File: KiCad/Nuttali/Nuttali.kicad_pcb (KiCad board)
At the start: 2 copper layers, 52.7 x 101.7 mm, 85 parts, among them J1 SWD, J2 B4B-XH-A, SW1 SW_DPST_x2, SW10 SW_Push, SW2 RND 210-00662, SW3 SW_Push, SW4 SW_Push, SW5 SW_Push, SW6 SW_Push, SW7 SW_Push, SW8 Rotary_Encoder, U1 STM32F411RETx, U2 PMW3389, U3 USBLC6-2P6, U4 AP131-15, U5 AP1117-15, Y1 16Mhz

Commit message: Working on the new pcb
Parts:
- removed D1, D4: LED, LED_SMD:LED_0201_0603Metric_Pad0.64x0.40mm_HandSolder
- added J3: Conn_01x03_Male, Connector_PinSocket_2.54mm:PinSocket_1x03_P2.54mm_Vertical, F.Cu at (192.0, 117.3)
- added J4: Conn_01x03_Male, Connector_PinSocket_2.54mm:PinSocket_1x03_P2.54mm_Vertical, F.Cu at (192.0, 99.8)
- moved D5 132.8 mm to (252.0, 145.3)
- moved R17 132.8 mm to (250.0, 149.3)
- moved R16 130.1 mm to (247.0, 153.3)
- moved R18 128.1 mm to (244.0, 143.3)
- moved R21 97.7 mm to (242.0, 44.3)
- moved R20 93.6 mm to (247.0, 48.3)
- moved D6 93.5 mm to (242.0, 51.3)
- moved R19 93.5 mm to (243.0, 47.3)
- moved U4 93.2 mm to (213.0, 82.3)
- moved R22 89.0 mm to (251.0, 70.3)
- moved R5 87.9 mm to (214.0, 78.3), turned to 90 degrees
- moved R23 85.0 mm to (251.0, 73.3)
- moved C13 84.4 mm to (221.0, 107.3), turned to 0 degrees
- moved C20 82.5 mm to (212.0, 78.4), turned to 90 degrees
- moved R4 81.5 mm to (210.0, 82.3), turned to 270 degrees
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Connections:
- R10 pad 2: SideBack -> Net-(J4-Pad2)
- R9 pad 2: SideFront -> Net-(J4-Pad3)
- SW5 pad 1: VDDIO_3.3V -> Net-(J4-Pad1)
- SW6 pad 1: VDDIO_3.3V -> Net-(J4-Pad1)
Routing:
- net GND: track 396.6 -> 74.1 mm, vias 18 -> 6
- net G_LED: track 199.4 -> 3.38 mm, vias 8 -> 0
- net R_LED: track 186.2 -> 5.65 mm, vias 6 -> 0
- net B_LED: track 171.9 -> 3.43 mm, vias 4 -> 0
- net Net-(R9-Pad1): track 78.9 -> 3.90 mm
- net Net-(R10-Pad1): track 70.1 -> 1.27 mm
- net VDDIO_3.3V: track 314.2 -> 268.6 mm, vias 10 -> 11
- net WheelB: track 87.5 -> 49.0 mm
- net +5V: track 80.1 -> 43.3 mm, vias 0 -> 1
- net WheelA: track 86.4 -> 54.4 mm
- net WheelButton: track 70.7 -> 40.0 mm
- net RightB: track 114.9 -> 90.9 mm
- net Turbo: track 63.6 -> 44.4 mm, vias 0 -> 2
- net NCS: track 44.7 -> 62.6 mm, vias 3 -> 4
- net MISO: track 41.6 -> 58.0 mm, vias 0 -> 2
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- removed copper zone on B.Cu, net GND
- removed copper zone on F.Cu, net GND
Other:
- board size 52.7 x 101.7 mm -> 38 x 78 mm

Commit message: Soon done with the pcb
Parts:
- removed D6, D7: LED_RGB, LED_SMD:LED_RGB_5050-6
- removed R19, R20, R21, R22, R23, R24: 220, Resistor_SMD:R_0805_2012Metric_Pad1.20x1.40mm_HandSolder
- added D4: LED, LED_SMD:LED_0201_0603Metric_Pad0.64x0.40mm_HandSolder, F.Cu at (195.0, 116.9)
- moved R16 76.2 mm to (222.0, 81.3), turned to 270 degrees
- moved R17 72.8 mm to (224.0, 81.3), turned to 270 degrees
- moved R18 64.6 mm to (226.0, 81.3), turned to 270 degrees
- moved D5 64.4 mm to (224.0, 87.3), turned to 270 degrees
- moved TP1 34.0 mm to (199.0, 73.3)
- moved J4 31.0 mm to (161.0, 99.8)
- moved R10 24.0 mm to (160.0, 94.3)
- moved R9 24.0 mm to (158.0, 94.3)
- moved SW5 24.0 mm to (163.3, 85.3)
- moved SW6 24.0 mm to (163.3, 92.3)
- moved R13 21.2 mm to (221.0, 66.3)
- moved SW7 13.0 mm to (221.0, 62.3), turned to 270 degrees
- moved TP8 12.6 mm to (215.0, 136.3)
- moved TP7 11.7 mm to (212.0, 136.3)
- moved C30 11.2 mm to (194.0, 69.3), turned to 0 degrees
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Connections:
- R10 pad 2: Net-(J4-Pad2) -> SideBack
- R9 pad 2: Net-(J4-Pad3) -> SideFront
- SW5 pad 1: Net-(J4-Pad1) -> VDDIO_3.3V
- SW6 pad 1: Net-(J4-Pad1) -> VDDIO_3.3V
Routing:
- net GND: track 74.1 -> 202.0 mm, vias 6 -> 21
- net VDDIO_3.3V: track 268.6 -> 377.7 mm, vias 11 -> 7
- net B_LED: track 3.43 -> 52.5 mm, vias 0 -> 2
- net G_LED: track 3.38 -> 51.4 mm, vias 0 -> 2
- net R_LED: track 5.65 -> 49.2 mm, vias 0 -> 2
- net WheelButton: track 40.0 -> 79.2 mm
- net Net-(R11-Pad2): track 0.00 -> 17.2 mm
- net Net-(R15-Pad1): track 15.0 -> 2.14 mm
- net Net-(R12-Pad2): track 0.00 -> 10.9 mm
- net Net-(J4-Pad1): track 8.85 -> 0.00 mm
- net WheelB: track 49.0 -> 56.6 mm
- net Net-(R13-Pad1): track 9.61 -> 2.31 mm
- net RightB: track 90.9 -> 98.1 mm, vias 2 -> 0
- net Turbo: track 44.4 -> 50.5 mm, vias 2 -> 0
- net Net-(R9-Pad1): track 3.90 -> 0.00 mm
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- added copper zone on B.Cu, net GND
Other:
- outline, holes or cut-outs redrawn
- net class powe_smal added: clearance 0.2, trace_width 0.4, via_dia 0.8, via_drill 0.4

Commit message: pushing a few things
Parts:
- moved TP6 1.00 mm to (226.0, 101.3)
- moved TP7 1.00 mm to (212.0, 135.3)
- moved TP8 1.00 mm to (215.0, 135.3)
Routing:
- net +5V: track 43.2 -> 118.5 mm, vias 1 -> 4
- net GND: track 202.0 -> 257.6 mm, vias 21 -> 24
- net R_LED: track 49.2 -> 46.9 mm
- net G_LED: track 51.4 -> 49.6 mm
- net WheelB: track 56.6 -> 58.3 mm

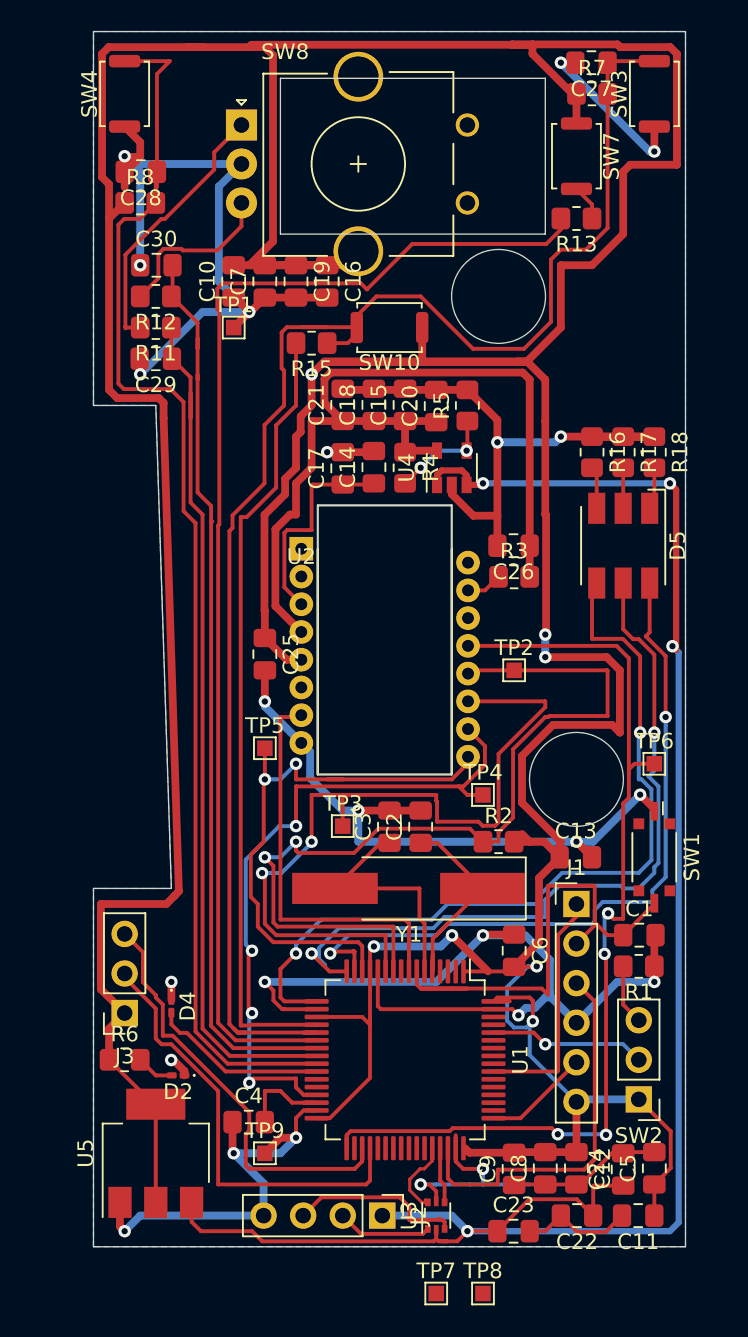
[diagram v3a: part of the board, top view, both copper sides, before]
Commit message: extended the pcb board with 2 mm to right
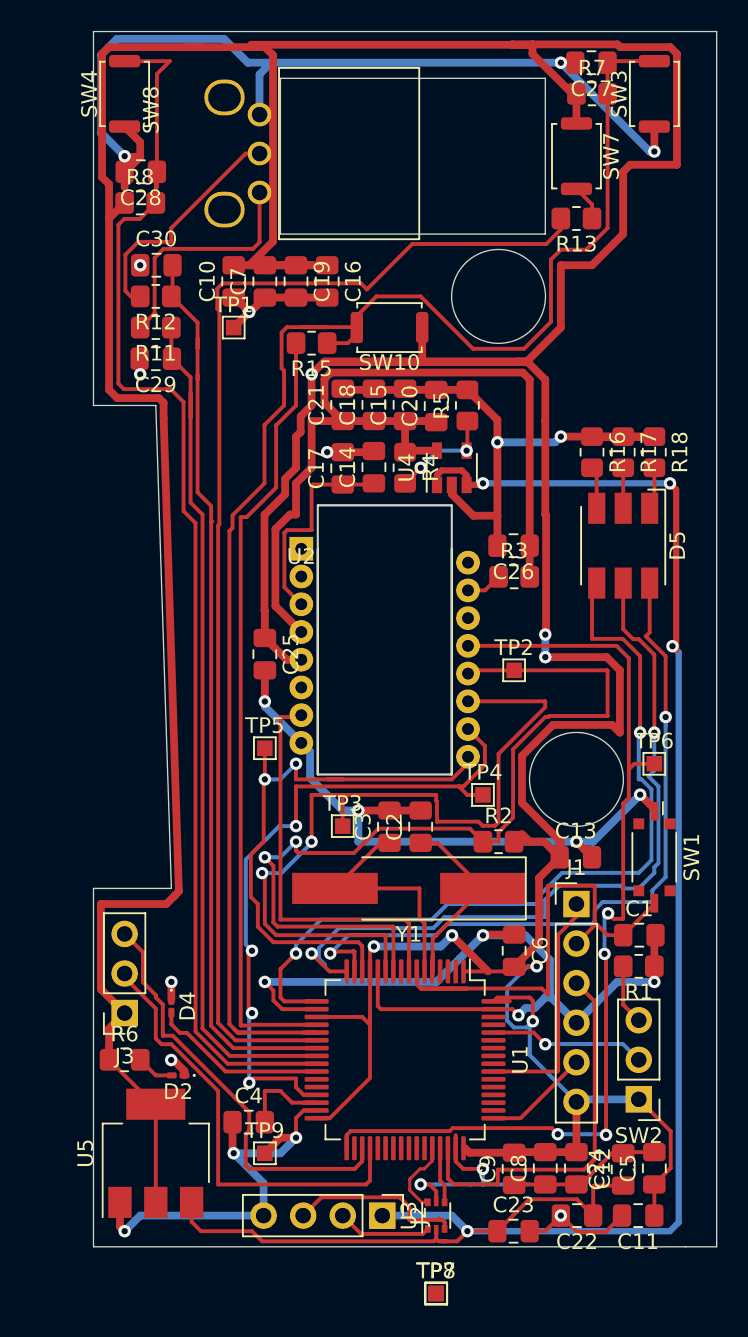
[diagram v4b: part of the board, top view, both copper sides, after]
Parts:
- SW8: footprint Rotary_Encoder:RotaryEncoder_Alps_EC11E_Vertical_H20mm_CircularMountingHoles -> PMW:Encoder
- moved TP8 3.00 mm to (212.0, 135.3)
- moved SW8 2.13 mm to (198.4, 62.1), turned to 90 degrees
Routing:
- net GND: track 257.6 -> 265.0 mm, vias 24 -> 25
- net VDDIO_3.3V: track 377.7 -> 373.1 mm
- net Net-(R12-Pad2): track 10.9 -> 15.2 mm
- net Net-(R11-Pad2): track 17.2 -> 15.2 mm
- removed copper zone on B.Cu, net GND
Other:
- board size 38 x 78 mm -> 40 x 78 mm
